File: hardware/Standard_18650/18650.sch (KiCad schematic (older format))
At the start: 56 parts, among them J2 Battery, J3 GPIO, J4 USB_B_Micro, J5 Power, J6 LEDs, J7 GPIO, Q1 BSS806N, Q2 BSS806N, Q3 BSS806N, Q4 BSS806N, SW1 Mode, SW2 Power, U1 STM32F411CE, U2 AP2210N-3.3TRG1, U3 BQ21040, U4 ESD7002WTT1G, Y1 24Mhz

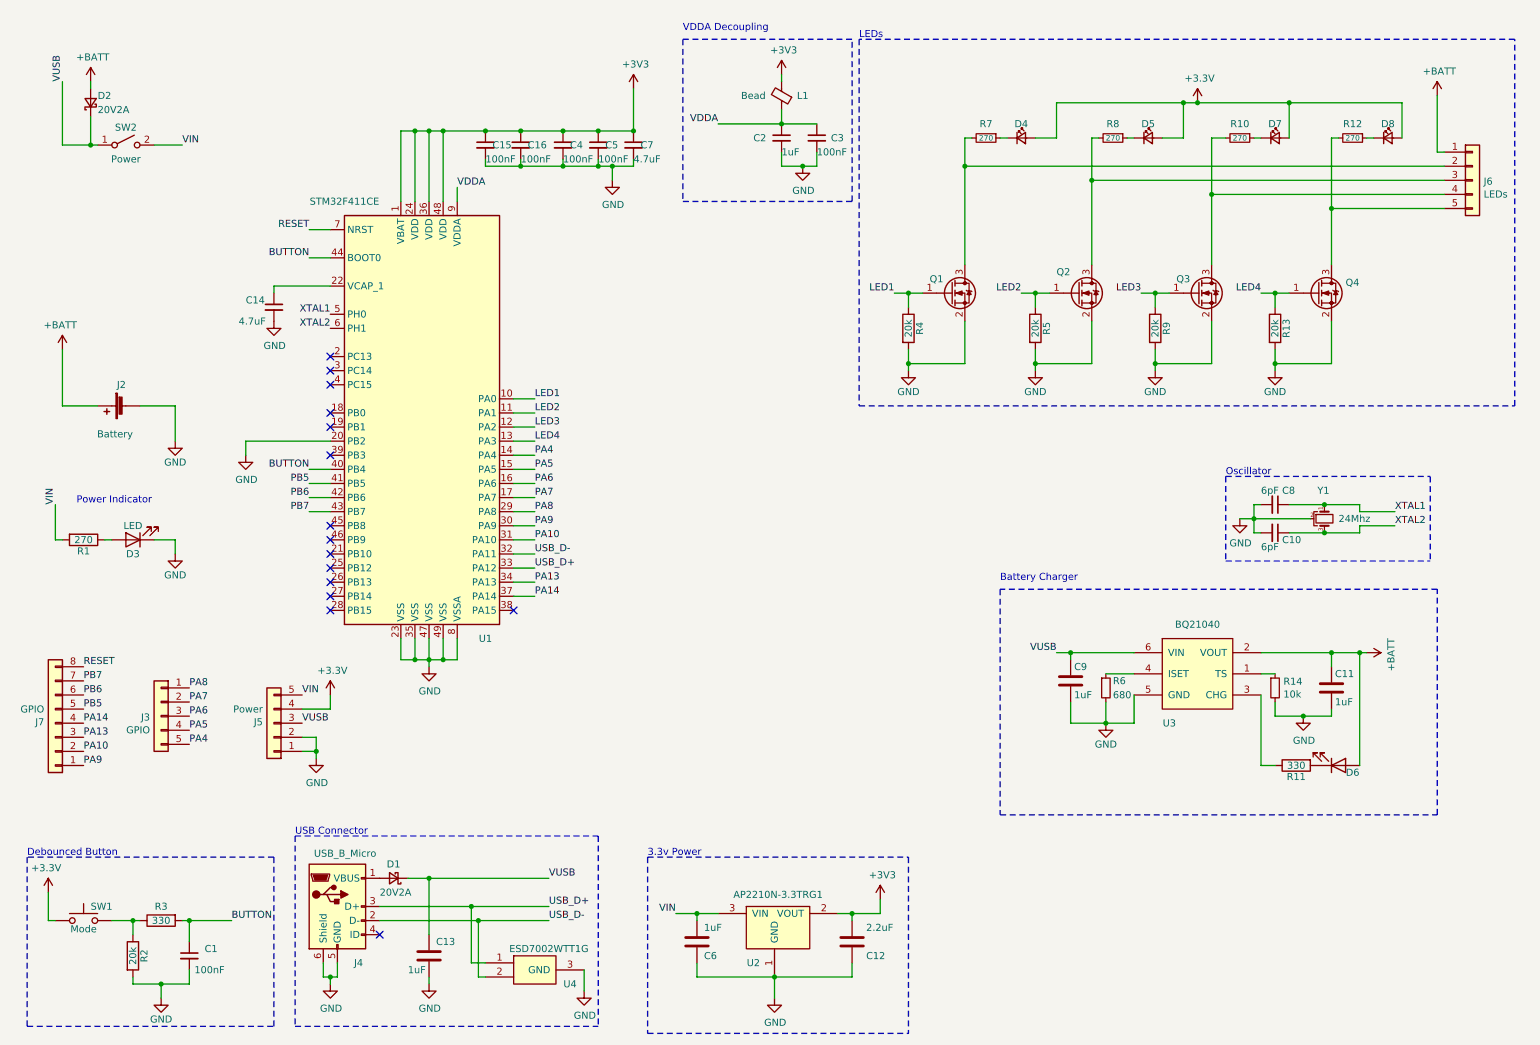
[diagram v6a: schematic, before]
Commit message: Add flash chip
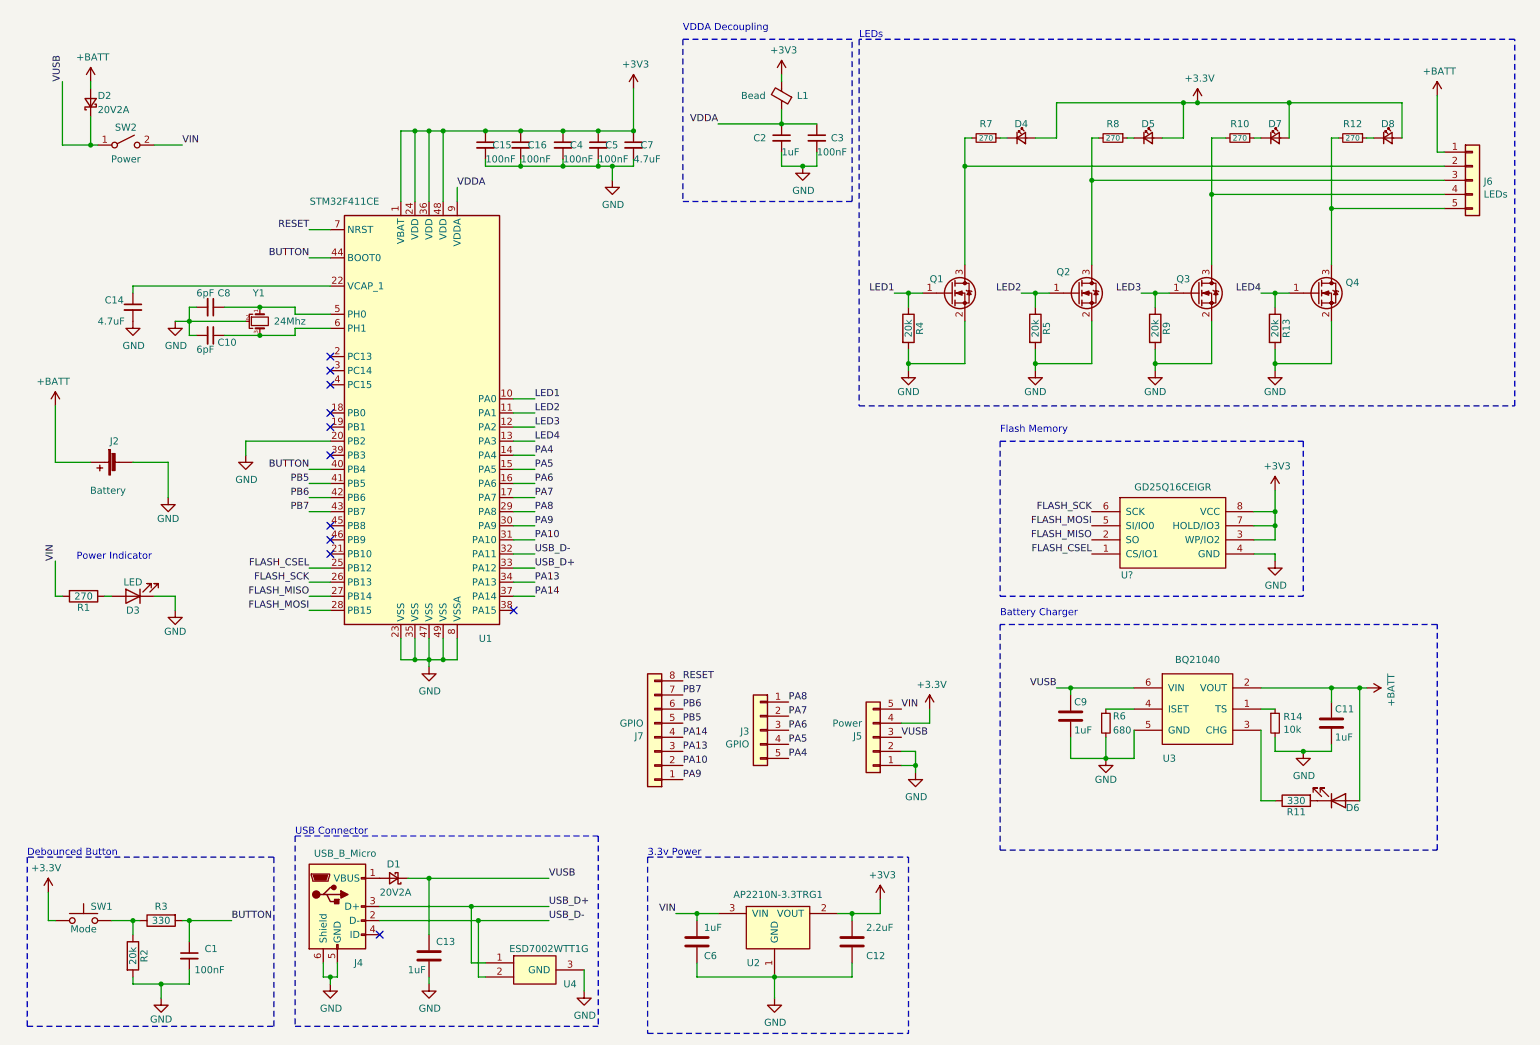
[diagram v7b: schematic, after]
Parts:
- added U?: GD25Q16CEIGR, Package_DFN_QFN:DFN-8-1EP_3x2mm_P0.5mm_EP1.3x1.5mm, symbol Jeremy:GD25Q16CEIGR
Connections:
- net +3V3: now also U?.3 (WP/IO2), U?.7 (HOLD/IO3), U?.8 (VCC)
- net GND: now also U?.4 (GND)
- net FLASH_CSEL: now reaches U1.25 (PB12)
- net FLASH_CSEL: now also U?.1 (CS/IO1)
- net FLASH_SCK: now reaches U1.26 (PB13)
- net FLASH_SCK: now also U?.6 (SCK)
- net FLASH_MISO: now reaches U1.27 (PB14)
- net FLASH_MISO: now also U?.2 (SO)
- net FLASH_MOSI: now reaches U1.28 (PB15)
- net FLASH_MOSI: now also U?.5 (SI/IO0)
- net XTAL1: no longer names the net of C8.1, U1.5 (PH0), Y1.1
- net XTAL2: no longer names the net of C10.1, U1.6 (PH1), Y1.3
- no-connect marks 15 -> 11
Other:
- note added: "Flash Memory"
- note removed: "Oscillator"
- moved on the sheet: C10, C11, C14, C8, C9, D3, D6, J2, J3, J5, J7, R1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

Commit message: Add RGB LED & Flash. Change power switch.
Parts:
- removed R6: 680, Resistor_SMD:R_0603_1608Metric, symbol Device:R_Small
- removed U3: BQ21040, Package_TO_SOT_SMD:SOT-23-6, symbol Jeremy:BQ21040
- removed U?: GD25Q16CEIGR, Package_DFN_QFN:DFN-8-1EP_3x2mm_P0.5mm_EP1.3x1.5mm, symbol Jeremy:GD25Q16CEIGR
- added D9: APA102-2020, LED_SMD:LED-APA102-2020, symbol LED:APA102-2020
- added U3: MCP73830, Package_DFN_QFN:DFN-6-1EP_2x2mm_P0.5mm_EP0.61x1.42mm, symbol jg_Battery_Management:MCP73830
- added U5: GD25Q16CEIGR, Package_DFN_QFN:DFN-8-1EP_3x2mm_P0.5mm_EP1.3x1.5mm, symbol Jeremy:GD25Q16CEIGR
- C11, C9: value 1uF -> 4.7uF; symbol Device:C -> Device:C_Small
- D1, D2: footprint Diode_SMD:D_SOD-323_HandSoldering -> Diode_SMD:D_SOD-323
- D6: symbol Device:LED -> Device:LED_Small
- R11: symbol Device:R -> Device:R_Small
- R14: value 10k -> 1k
- SW1: footprint Button_Switch_SMD:SW_SPST_FSMSM -> Jeremy Button/Switch:SW_SPST_FSMSM
- SW2: footprint Button_Switch_THT:SW_CW_GPTS203211B -> Jeremy:Switch_L068-A-DC30V1A; MPN GPTS203211B -> L068-A
- U1: footprint Package_DFN_QFN:QFN-48-1EP_7x7mm_P0.5mm_EP5.6x5.6mm -> Jeremy:QFN-48-1EP_7x7mm_P0.5mm_EP5.6x5.6mm
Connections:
- net +3V3: now also D9.1 (VDD), U5.3 (WP/IO2), U5.7 (HOLD/IO3), U5.8 (VCC)
- net +BATT: now also U3.3 (VBAT); no longer D6.2 (A)
- net FLASH_CSEL: now also U5.1 (CS/IO1)
- net FLASH_MISO: now also U5.2 (SO)
- net FLASH_MOSI: now also U5.5 (SI/IO0)
- net FLASH_SCK: now also U5.6 (SCK)
- net GND: now also D9.6 (GND), U3.1 (VSS), U5.4 (GND)
- net VUSB: now also D1.2 (A), D6.2 (A), J4.1 (VBUS), U3.4 (VDD); no longer D1.1 (K), D2.1 (K), SW2.1 (A)
- net at R14.1: now also U3.6 (PROG)
- net at R11.1: now also D6.1 (K)
- net at R11.2: now also U3.2 (STAT); no longer D6.1 (K)
- net RGB_CKI: now reaches U1.18 (PB0)
- net RGB_CKI: now also D9.5 (CKI)
- net RGB_SDI: now reaches U1.45 (PB8)
- net RGB_SDI: now also D9.4 (SDI)
- new net: D1.1 (K), D2.1 (K), SW2.1 (A)
- no-connect marks 11 -> 12
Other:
- note added: "RGB Status LED"
- moved on the sheet: C11, C14, C9, D1, D3, D4, D5, D6, D7, D8, J2, J3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
